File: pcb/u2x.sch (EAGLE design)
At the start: 9 parts, among them IC4 REG1117, SW20 324_SW, U1 UG-2864HSWEG01, U2 CY8C5868LTI-LP039, U3 USBC_16P

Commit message: started working on pcb
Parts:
- removed U1: UG-2864HSWEG01, lul:LUL_DISP_OLED_UG-2864HSWEG01
- removed X2: (no value), bott:USB-A-H
- added JP1: (no value), adafruit_changed:PINHD-2X20-BIG
- added X8: USB2, RPB:USB2
- X1: value (none) -> USB2; device bott:USB-A-H -> RPB:USB2
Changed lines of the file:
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@@
 <parts>
 <part name="U3" library="my_usbc_16p" deviceset="USBC_16P" device=""/>
-<part name="U1" library="lul" deviceset="LUL_DISP_OLED_UG-2864HSWEG01" device="" value="UG-2864HSWEG01"/>
 <part name="SD1" library="clock" deviceset="TF-HOLDER" device=""/>
 <part name="IC4" library="clock" deviceset="REG1117" device=""/>
 <part name="SW20" library="3pos_slide_switch_centered" deviceset="324_SW" device="" value="324_SW"/>
-<part name="X1" library="bott" deviceset="USB" device="-A-H"/>
-<part name="X2" library="bott" deviceset="USB" device="-A-H"/>
 <part name="X3" library="bott" deviceset="USB" device="-A-H"/>
 <part name="U2" library="SparkFun-IC-Microcontroller" deviceset="PSOC_5LP_68QFN" device="" value="CY8C5868LTI-LP039"/>
+<part name="JP1" library="adafruit_changed" deviceset="PINHD-2X20" device="-BIG"/>
+<part name="X8" library="RPB" deviceset="USB2" device=""/>
+<part name="X1" library="RPB" deviceset="USB2" device=""/>
 </parts>
 <sheets>
@@
 <instances>
 <instance part="U3" gate="G$1" x="-2.54" y="101.6" smashed="yes" rot="MR0"/>
-<instance part="U1" gate="G$1" x="68.58" y="104.14" smashed="yes">
-<attribute name="NAME" x="45.72" y="144.78" size="1.27" layer="95" font="vector"/>
-<attribute name="VALUE" x="45.72" y="60.96" size="1.27" layer="96" font="vector"/>
-</instance>
 <instance part="SD1" gate="G$1" x="-76.2" y="81.28" smashed="yes" rot="MR0">
 <attribute name="NAME" x="-71.12" y="94.488" size="1.6764" layer="95" rot="MR0"/>
@@
 </instance>
 <instance part="SW20" gate="G$1" x="-111.76" y="137.16" smashed="yes" rot="MR270"/>
-<instance part="X1" gate="G$1" x="-35.56" y="66.04" smashed="yes">
-<attribute name="NAME" x="-35.56" y="60.96" size="1.27" layer="95"/>
-</instance>
-<instance part="X2" gate="G$1" x="-22.86" y="66.04" smashed="yes">
-<attribute name="NAME" x="-22.86" y="60.96" size="1.27" layer="95"/>
-</instance>
 <instance part="X3" gate="G$1" x="-5.08" y="66.04" smashed="yes">
 <attribute name="NAME" x="-5.08" y="60.96" size="1.27" layer="95"/>
@@
 <attribute name="VALUE" x="-25.4" y="147.32" size="1.778" layer="96"/>
 </instance>
+<instance part="JP1" gate="A" x="-73.66" y="180.34" smashed="yes">
+<attribute name="NAME" x="-80.01" y="206.375" size="1.778" layer="95"/>
+<attribute name="VALUE" x="-80.01" y="149.86" size="1.778" layer="96"/>
+</instance>
+<instance part="X8" gate="A" x="50.8" y="132.08" smashed="yes" rot="R270">
+<attribute name="NAME" x="59.69" y="134.62" size="1.778" layer="95" rot="R270"/>
+<attribute name="VALUE" x="43.18" y="134.62" size="1.778" layer="96" rot="R270"/>
+</instance>
+<instance part="X8" gate="B" x="76.2" y="132.08" smashed="yes" rot="R270">
+<attribute name="NAME" x="85.09" y="134.62" size="1.778" layer="95" rot="R270"/>
+<attribute name="VALUE" x="68.58" y="134.62" size="1.778" layer="96" rot="R270"/>
+</instance>
+<instance part="X8" gate="S" x="96.52" y="132.08" smashed="yes">
+<attribute name="NAME" x="104.14" y="129.54" size="1.778" layer="95"/>
+</instance>
+<instance part="X1" gate="A" x="76.2" y="109.22" smashed="yes" rot="R270">
+<attribute name="NAME" x="85.09" y="111.76" size="1.778" layer="95" rot="R270"/>
+<attribute name="VALUE" x="68.58" y="111.76" size="1.778" layer="96" rot="R270"/>
+</instance>
+<instance part="X1" gate="B" x="55.88" y="109.22" smashed="yes" rot="R270">
+<attribute name="NAME" x="64.77" y="111.76" size="1.778" layer="95" rot="R270"/>
+<attribute name="VALUE" x="48.26" y="111.76" size="1.778" layer="96" rot="R270"/>
+</instance>
 </instances>

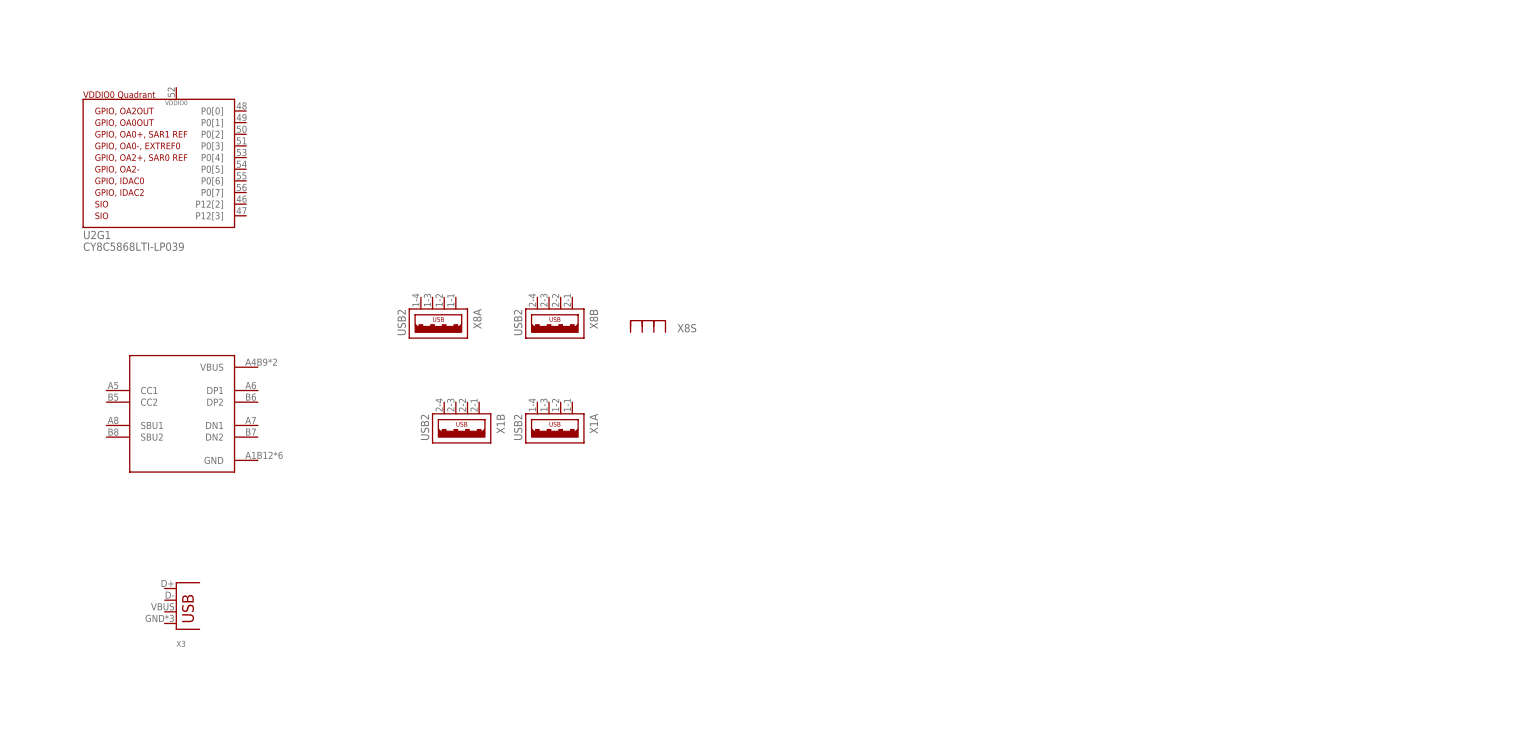
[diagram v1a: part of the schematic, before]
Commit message: f1c100s library done
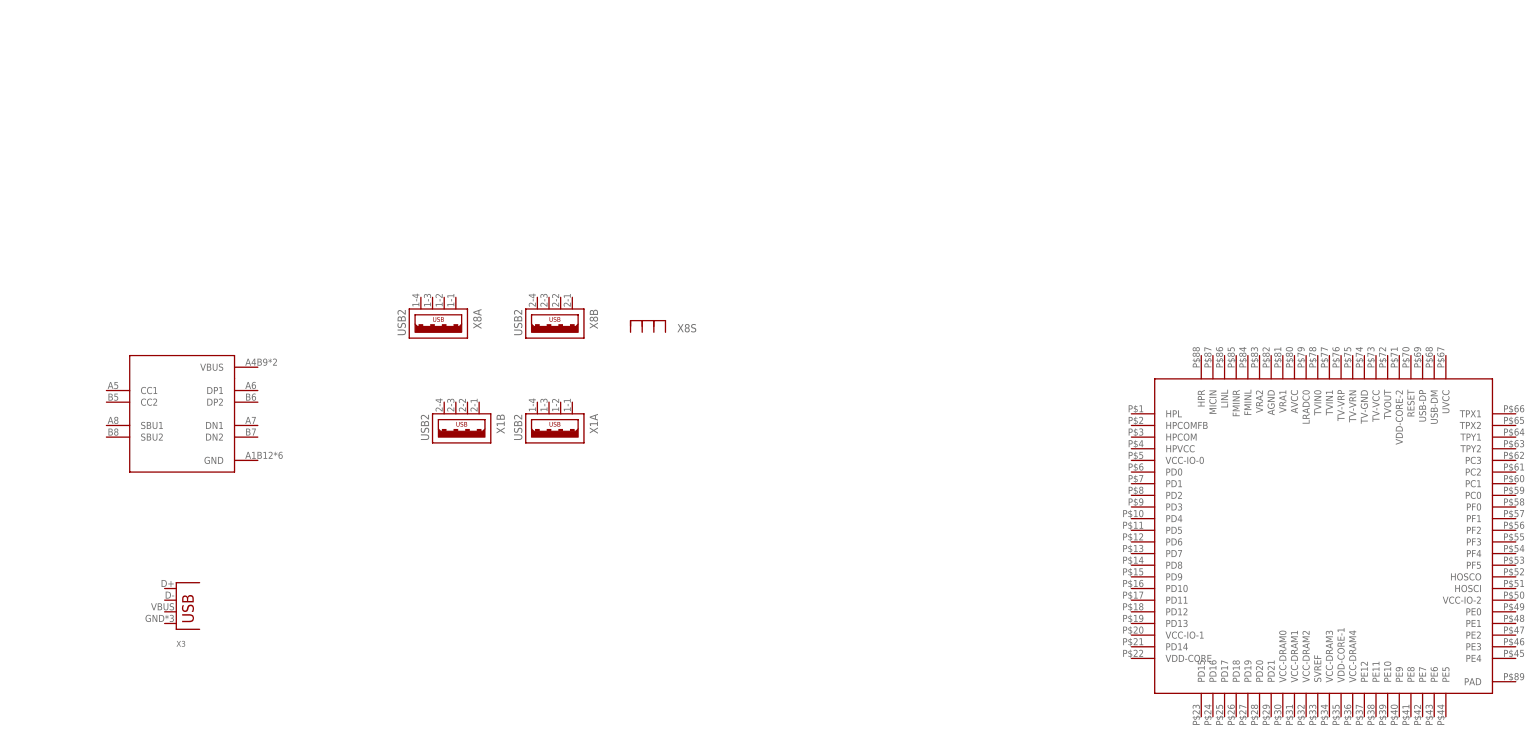
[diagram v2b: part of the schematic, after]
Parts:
- removed U2: CY8C5868LTI-LP039, SparkFun-IC-Microcontroller:PSOC_5LP_68QFN
- added U$1: F1C100S_DEV, f1c100s:F1C100S_DEV
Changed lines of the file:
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@@
 <part name="SW20" library="3pos_slide_switch_centered" deviceset="324_SW" device="" value="324_SW"/>
 <part name="X3" library="bott" deviceset="USB" device="-A-H"/>
-<part name="U2" library="SparkFun-IC-Microcontroller" deviceset="PSOC_5LP_68QFN" device="" value="CY8C5868LTI-LP039"/>
 <part name="JP1" library="adafruit_changed" deviceset="PINHD-2X20" device="-BIG"/>
 <part name="X8" library="RPB" deviceset="USB2" device=""/>
 <part name="X1" library="RPB" deviceset="USB2" device=""/>
+<part name="U$1" library="f1c100s" deviceset="F1C100S_DEV" device=""/>
 </parts>
 <sheets>
@@
 <instance part="X3" gate="G$1" x="-5.08" y="66.04" smashed="yes">
 <attribute name="NAME" x="-5.08" y="60.96" size="1.27" layer="95"/>
-</instance>
-<instance part="U2" gate="G1" x="-25.4" y="152.4" smashed="yes">
-<attribute name="NAME" x="-25.4" y="149.86" size="1.778" layer="95"/>
-<attribute name="VALUE" x="-25.4" y="147.32" size="1.778" layer="96"/>
 </instance>
 <instance part="JP1" gate="A" x="-73.66" y="180.34" smashed="yes">
@@
 <attribute name="VALUE" x="48.26" y="111.76" size="1.778" layer="96" rot="R270"/>
 </instance>
+<instance part="U$1" gate="G$1" x="243.84" y="83.82" smashed="yes"/>
 </instances>
 <busses>

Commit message: added more resources, worked on PCB, new libraries, placement, USB chip selection, OLED libarary
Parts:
- removed IC4: REG1117, clock:REG1117
- added IC1: LD117AS33TR, v-reg:LD117AS33TR
- added IC2: LD117AS25TR, v-reg:LD117AS25TR
- added IC3: LD117AS12TR, v-reg:LD117AS12TR
- added U$2, U$3, U$4, U$5: M2.5HOLE, f1c100s:M2.5HOLE
- added U1: USB251XB, USB251xB:USB251XB
- added U2: (no value), lul:LUL_DISP_OLED_UG-2864HSWEG01
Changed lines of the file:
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@@
 <layer number="117" name="secv21" color="7" fill="1" visible="yes" active="yes"/>
 <layer number="118" name="Rect_Pads" color="7" fill="1" visible="yes" active="yes"/>
+<layer number="119" name="PF_Ref" color="7" fill="1" visible="no" active="no"/>
 <layer number="120" name="120" color="7" fill="1" visible="yes" active="yes"/>
 <layer number="121" name="_tsilk" color="7" fill="1" visible="yes" active="yes"/>
@@
 <layer number="131" name="tAdjust" color="7" fill="1" visible="yes" active="yes"/>
 <layer number="132" name="bAdjust" color="7" fill="1" visible="yes" active="yes"/>
+<layer number="133" name="bottom_silk" color="7" fill="1" visible="yes" active="yes"/>
+<layer number="134" name="silk_top" color="7" fill="1" visible="yes" active="yes"/>
+<layer number="135" name="silk_bottom" color="7" fill="1" visible="yes" active="yes"/>
+<layer number="136" name="silktop" color="7" fill="1" visible="yes" active="yes"/>
+<layer number="137" name="silkbottom" color="7" fill="1" visible="yes" active="yes"/>
+<layer number="138" name="EEE" color="7" fill="1" visible="yes" active="yes"/>
+<layer number="139" name="_tKeepout" color="7" fill="1" visible="yes" active="yes"/>
+<layer number="140" name="mbKeepout" color="7" fill="1" visible="yes" active="yes"/>
+<layer number="141" name="ASSEMBLY_TOP" color="7" fill="1" visible="yes" active="yes"/>
+<layer number="142" name="mbRestrict" color="7" fill="1" visible="yes" active="yes"/>
+<layer number="143" name="PLACE_BOUND_TOP" color="7" fill="1" visible="yes" active="yes"/>
 <layer number="144" name="Drill_legend" color="7" fill="1" visible="yes" active="yes"/>
 <layer number="145" name="DrillLegend_01-02" color="7" fill="1" visible="yes" active="yes"/>
@@
 <layer number="154" name="FabDoc2" color="7" fill="1" visible="yes" active="yes"/>
 <layer number="155" name="FabDoc3" color="7" fill="1" visible="yes" active="yes"/>
+<layer number="166" name="AntennaArea" color="7" fill="1" visible="yes" active="yes"/>
+<layer number="168" name="4mmHeightArea" color="7" fill="1" visible="yes" active="yes"/>
+<layer number="191" name="mNets" color="7" fill="1" visible="yes" active="yes"/>
+<layer number="192" name="mBusses" color="7" fill="1" visible="yes" active="yes"/>
+<layer number="193" name="mPins" color="7" fill="1" visible="yes" active="yes"/>
+<layer number="194" name="mSymbols" color="7" fill="1" visible="yes" active="yes"/>
+<layer number="195" name="mNames" color="7" fill="1" visible="yes" active="yes"/>
+<layer number="196" name="mValues" color="7" fill="1" visible="yes" active="yes"/>
 <layer number="199" name="Contour" color="7" fill="1" visible="yes" active="yes"/>
 <layer number="200" name="200bmp" color="1" fill="10" visible="no" active="no"/>
@@
 <part name="U3" library="my_usbc_16p" deviceset="USBC_16P" device=""/>
 <part name="SD1" library="clock" deviceset="TF-HOLDER" device=""/>
-<part name="IC4" library="clock" deviceset="REG1117" device=""/>
 <part name="SW20" library="3pos_slide_switch_centered" deviceset="324_SW" device="" value="324_SW"/>
 <part name="X3" library="bott" deviceset="USB" device="-A-H"/>
@@
 <part name="X1" library="RPB" deviceset="USB2" device=""/>
 <part name="U$1" library="f1c100s" deviceset="F1C100S_DEV" device=""/>
+<part name="IC1" library="v-reg" library_urn="urn:adsk.eagle:library:409" deviceset="LD117A?*" device="S" package3d_urn="urn:adsk.eagle:package:30370/1" technology="33TR" value="LD117AS33TR"/>
+<part name="IC2" library="v-reg" library_urn="urn:adsk.eagle:library:409" deviceset="LD117A?*" device="S" package3d_urn="urn:adsk.eagle:package:30370/1" technology="25TR" value="LD117AS25TR"/>
+<part name="IC3" library="v-reg" library_urn="urn:adsk.eagle:library:409" deviceset="LD117A?*" device="S" package3d_urn="urn:adsk.eagle:package:30370/1" technology="12TR" value="LD117AS12TR"/>
+<part name="U$2" library="f1c100s" deviceset="M2.5HOLE" device=""/>
+<part name="U$3" library="f1c100s" deviceset="M2.5HOLE" device=""/>
+<part name="U$4" library="f1c100s" deviceset="M2.5HOLE" device=""/>
+<part name="U$5" library="f1c100s" deviceset="M2.5HOLE" device=""/>
+<part name="U1" library="USB251xB" deviceset="USB251XB" device=""/>
+<part name="U2" library="lul" deviceset="LUL_DISP_OLED_UG-2864HSWEG01" device=""/>
 </parts>
 <sheets>
@@
 <attribute name="VALUE" x="-86.868" y="91.44" size="1.6764" layer="96" rot="MR270"/>
 </instance>
-<instance part="IC4" gate="G$1" x="-63.5" y="124.46" smashed="yes">
-<attribute name="NAME" x="-71.12" y="130.175" size="1.778" layer="95" ratio="10"/>
-<attribute name="VALUE" x="-68.58" y="127" size="1.778" layer="96" ratio="10"/>
-</instance>
 <instance part="SW20" gate="G$1" x="-111.76" y="137.16" smashed="yes" rot="MR270"/>
 <instance part="X3" gate="G$1" x="-5.08" y="66.04" smashed="yes">
@@
 </instance>
 <instance part="U$1" gate="G$1" x="243.84" y="83.82" smashed="yes"/>
+<instance part="IC1" gate="G$1" x="175.26" y="5.08" smashed="yes">
+<attribute name="NAME" x="177.8" y="-2.54" size="1.778" layer="95"/>
+<attribute name="VALUE" x="177.8" y="-5.08" size="1.778" layer="96"/>
+</instance>
+<instance part="IC2" gate="G$1" x="175.26" y="-17.78" smashed="yes">
+<attribute name="NAME" x="177.8" y="-25.4" size="1.778" layer="95"/>
+<attribute name="VALUE" x="177.8" y="-27.94" size="1.778" layer="96"/>
+</instance>
+<instance part="IC3" gate="G$1" x="218.44" y="5.08" smashed="yes">
+<attribute name="NAME" x="220.98" y="-2.54" size="1.778" layer="95"/>
+<attribute name="VALUE" x="220.98" y="-5.08" size="1.778" layer="96"/>
+</instance>
+<instance part="U$2" gate="G$1" x="68.58" y="71.12" smashed="yes"/>
+<instance part="U$3" gate="G$1" x="68.58" y="55.88" smashed="yes"/>
+<instance part="U$4" gate="G$1" x="68.58" y="40.64" smashed="yes"/>
+<instance part="U$5" gate="G$1" x="68.58" y="25.4" smashed="yes"/>
+<instance part="U1" gate="U1" x="66.04" y="-63.5" smashed="yes">
+<attribute name="NAME" x="48.26" y="-37.592" size="1.778" layer="95"/>
+<attribute name="VALUE" x="48.26" y="-98.806" size="1.778" layer="96"/>
+</instance>
+<instance part="U2" gate="G$1" x="238.76" y="-93.98" smashed="yes">
+<attribute name="NAME" x="218.44" y="-68.58" size="1.27" layer="95" font="vector"/>
+<attribute name="VALUE" x="218.44" y="-119.38" size="1.27" layer="96" font="vector"/>
+</instance>
 </instances>
 <busses>
@@
 </schematic>
 </drawing>
+<compatibility>
+<note version="6.3" minversion="6.2.2" severity="warning">
+Since Version 6.2.2 text objects can contain more than one line,
+which will not be processed correctly with this version.
+</note>
+<note version="8.2" severity="warning">
+Since Version 8.2, EAGLE supports online libraries. The ids
+of those online libraries will not be understood (or retained)
+with this version.
+</note>
+<note version="8.3" severity="warning">
+Since Version 8.3, EAGLE supports URNs for individual library
+assets (packages, symbols, and devices). The URNs of those assets
+will not be understood (or retained) with this version.
+</note>
+<note version="8.3" severity="warning">
+Since Version 8.3, EAGLE supports the association of 3D packages
+with devices in libraries, schematics, and board files. Those 3D
+packages will not be understood (or retained) with this version.
+</note>
+</compatibility>
 </eagle>

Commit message: added ch340, working on power
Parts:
- added C1, C2, C29, C3: 10uF, clock:CAP0805
- added C27: 47uF, clock:C-USC1210
- added LED1, LED3: (no value), adafruit:LEDCHIP-LED0805
- added R1, R9: 5.1K, joyAnalog:RESISTOR0805-RES
- added R3, R4: 1K, SparkFun-Passives:RESISTOR0805-RES
- added U5: CH340C, SparkFun-IC-Comms:CH340C
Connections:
- new net +3V3: C27.1, IC1.OUT, IC3.IN
- new net +5V: C1.2, C29.2, IC1.IN, IC2.IN, U3.VBUS
- new net GND: C1.1, C2.1, C27.2, C29.1, C3.1, IC1.ADJ, IC2.ADJ, IC3.ADJ, R1.2, R9.2, U3.GND
- new net N$1: R9.1, U3.CC1
- new net N$2: R1.1, U3.CC2
- new net N$3: C2.2, IC2.OUT
- new net N$4: C3.2, IC3.OUT
- new net N$5: LED1.C, R4.2
- new net N$6: LED3.C, R3.2
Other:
- moved on the sheet: IC1, IC2, IC3
